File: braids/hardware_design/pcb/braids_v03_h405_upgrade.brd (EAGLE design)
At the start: 78.7 x 106.7 mm, 97 parts, among them IC1 74HC595D, IC2 74HC595D, IC3 LM4040B25, IC4 LM4040B10, IC5 DAC8551, IC6 LM1117-5.0, IC8 MCP6004, IC9 TL072, Q1 MMBT3904, Q2 MMBT3904, Q3 MMBT3904, Q4 MMBT3904, Q6 MMBT3904, SW1 EC12E_SW

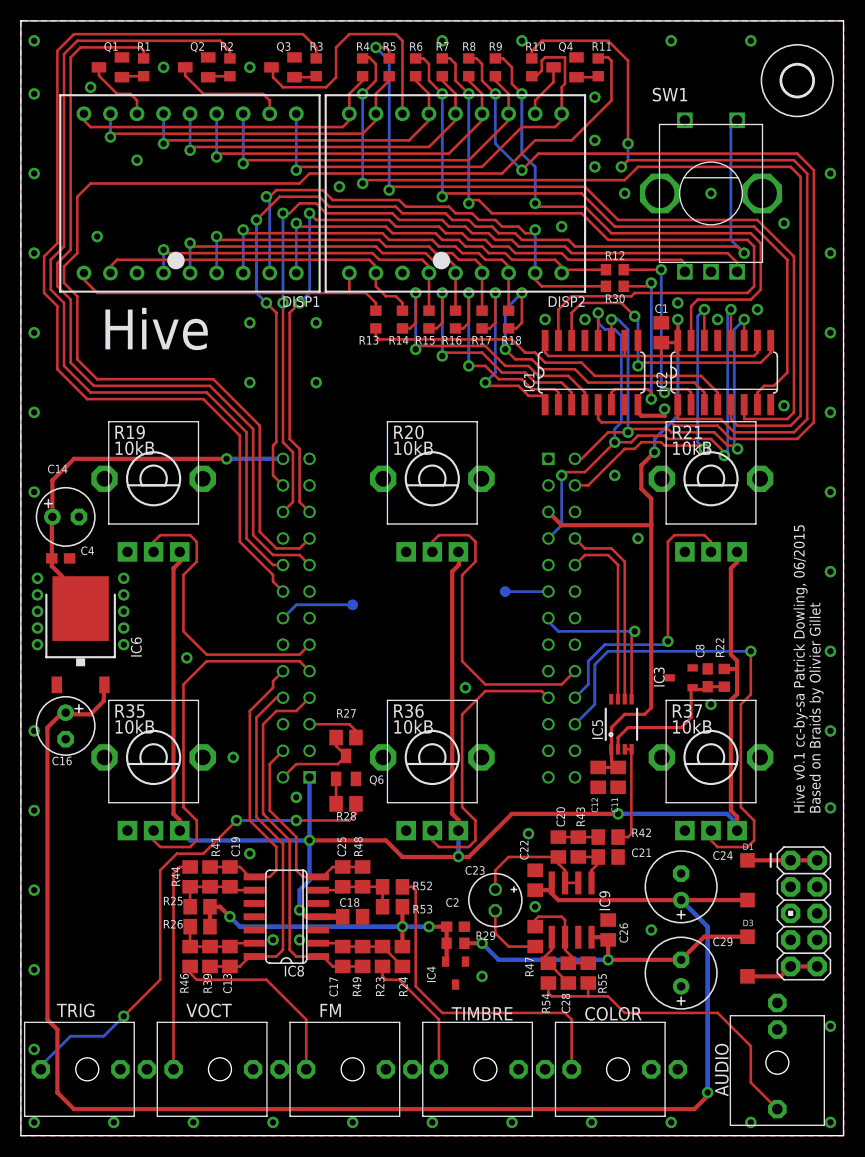
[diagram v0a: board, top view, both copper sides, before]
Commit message: Add switches and LEDs, DAC uses +3V3_A
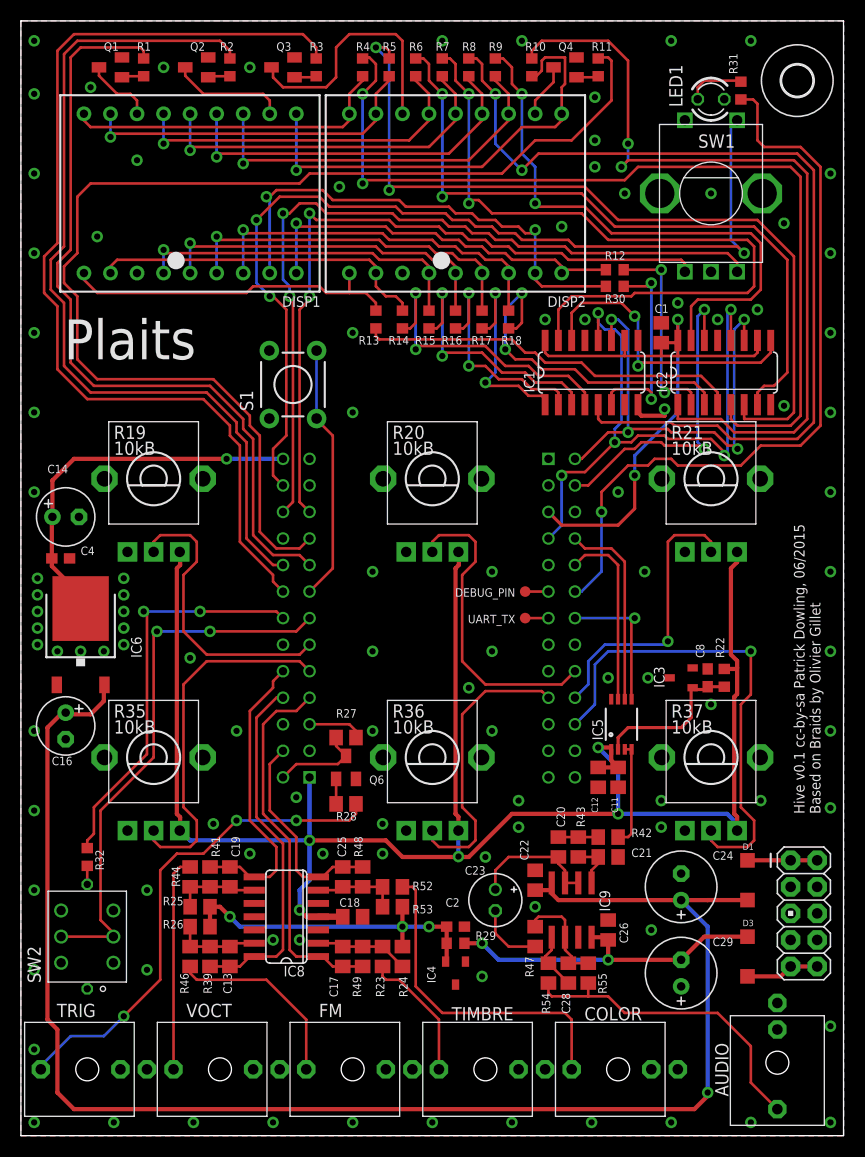
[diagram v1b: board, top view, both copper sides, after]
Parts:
- added LED1: (no value), led:LED3MM
- added R31, R32: 100, rcl:R0603
- added S1: (no value), SparkFun:TACTILE-PTH
- added SW2: LP4OA1PBCT, og-switch:LP4OA1PBCT
- moved TP1 16.6 mm to (48.3, 49.5), flipped to the top
- moved TP2 1.91 mm to (48.3, 52.1), flipped to the top, turned to 270 degrees
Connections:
- removed net 3V3A: C18.1, IC8.4, MCU.EXT2-1, R19.P$1, R20.P$1, R21.P$1, R22.1, R35.P$1, R36.P$1, R37.P$1
- new net +3V3_A: C11.1, C12.1, C18.1, IC5.1, IC8.4, MCU.EXT2-1, R19.P$1, R20.P$1, R21.P$1, R22.1, R35.P$1, R36.P$1, R37.P$1
- new net LED1: MCU.EXT1-12, R31.1
- new net LED2: MCU.EXT2-14, R32.2
- new net N$47: LED1.A, R31.2
- new net N$48: R32.1, SW2.L1
- new net SWITCH1: MCU.EXT2-15, S1.3, S1.4
- new net SWITCH2: MCU.EXT2-13, SW2.P2, SW2.P5
- net +3V3: no longer C11.1, C12.1, IC5.1
- net DAC_SS: now also MCU.EXT1-14; no longer MCU.EXT1-13
- net GND: now also LED1.K, S1.1, S1.2, SW2.L2, SW2.P3, SW2.P6
- net UART_LOGGER: now also MCU.EXT1-13; no longer MCU.EXT2-14
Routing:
- net +3V3_A: track 0.00 -> 174.5 mm, vias 0 -> 5
- net 3V3A: track 162.9 -> 0.00 mm, vias 4 -> 0
- net LED1: track 0.00 -> 72.2 mm, vias 0 -> 1
- net SWITCH2: track 0.00 -> 52.1 mm, vias 0 -> 2
- net LED2: track 0.00 -> 38.7 mm, vias 0 -> 2
- net +3V3: track 91.1 -> 60.1 mm
- net SWITCH1: track 0.00 -> 24.6 mm
- net N$47: track 0.00 -> 5.58 mm
- net UART_LOGGER: track 7.19 -> 2.22 mm
- net DAC_SS: track 15.6 -> 13.6 mm
- net DEBUG_PIN: track 4.13 -> 2.22 mm
- net N$48: track 0.00 -> 1.77 mm
- net ENC_CLICK: track 90.0 -> 91.0 mm
- net ENC_B: track 68.9 -> 68.1 mm
- net N$19: track 32.1 -> 32.7 mm
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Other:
- board text added: "Plaits"
- board text removed: "Hive"

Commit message: Re-assign some GPIOs due to conflicts on Olimex boards, some tweaks
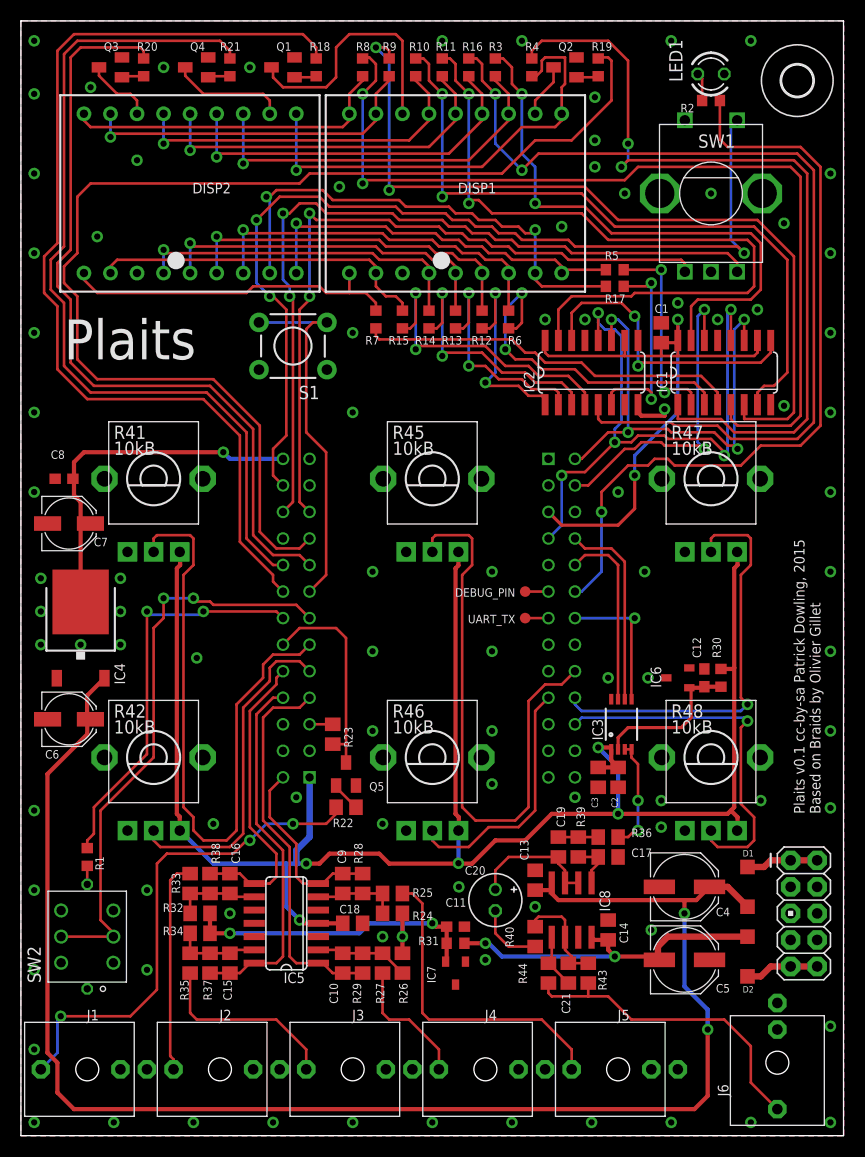
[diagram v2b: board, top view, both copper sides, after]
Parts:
- removed C22, C26: 100n, rcl:C0805
- removed C23: 10u, rcl:E2-5
- removed C24, C29: 47u, rcl:E2,5-7
- removed C25: 1n, rcl:C0805
- removed C28: 47p, rcl:C0805
- removed IC9: TL072, linear:SO08
- removed Q6: MMBT3904, transistor:SOT23-BEC
- removed R49: 66.5k, rcl:R0805
- removed R52, R55: 100k, rcl:R0805
- removed R53: 200k, rcl:R0805
- removed R54: 1k, rcl:R0805
- added C10, C15, C9: 1n, rcl:C0805
- added C3: 1u, rcl:C0805
- added C5: 47u, rcl:PANASONIC_D
- added C6, C7: 22u, rcl:PANASONIC_C
- added IC7: LM4040B10, texas:DBZ_R-PDSO-G3
- added Q5: MMBT3904, transistor:SOT23-BEC
- added R33: 100k, rcl:R0805
- added R34: 200k, rcl:R0805
- added R38: 33k, rcl:R0805
- added R40: 24.9k, rcl:R0805
- added R45: 10kB, pot-alps:ALPS_POT_VERTICAL_PS
- C11: device rcl:C0805 -> rcl:C0603
- C12: value 1u -> 470n; device rcl:C0805 -> rcl:C0603
- C13: value 1n -> 100n
- C14: value 22u -> 100n; device rcl:E2,5-6 -> rcl:C0805
- C16: value 22u -> 1n; device rcl:E2,5-6 -> rcl:C0805
- C17, C19: value 1n -> 100p
- C2: device rcl:C0603 -> rcl:C0805
- C20: value 100p -> 10u; device rcl:C0805 -> rcl:E2-5
- C21: value 100p -> 47p
- C4: value 100n -> 47u; device rcl:C0603 -> rcl:PANASONIC_D
- C8: value 470n -> 100n
- IC3: value LM4040B25 -> DAC8551; device texas:DBZ_R-PDSO-G3 -> og-dac:MSOP-8
- IC4: value LM4040B10 -> LM1117-5.0; device texas:DBZ_R-PDSO-G3 -> og-vreg:TO252
- IC5: value DAC8551 -> MCP6004; device og-dac:MSOP-8 -> gm-ics:SO14
- IC6: value LM1117-5.0 -> LM4040B25; device og-vreg:TO252 -> texas:DBZ_R-PDSO-G3
- IC8: value MCP6004 -> TL072; device gm-ics:SO14 -> linear:SO08
- MCU1: value STM32H103 -> STM32H405
- R1, R11, R2, R3: value 1k -> 100
- R18: value 100 -> 1k
- R19, R20, R21: value 10kB -> 1k; device pot-alps:ALPS_POT_VERTICAL_PS -> rcl:R0603
- R22: value 150 -> 100k; device rcl:R0603 -> rcl:R0805
- R23: value 100k -> 10k
- R27: value 10k -> 100k
- R28: value 100k -> 33k
- R29: value 470 -> 33k; device rcl:R0603 -> rcl:R0805
- R30: value 100 -> 150
- R31: value 100 -> 470
- R32: value 100 -> 100k; device rcl:R0603 -> rcl:R0805
- R35: value 10kB -> 100k; device pot-alps:ALPS_POT_VERTICAL_PS -> rcl:R0805
- R36: value 10kB -> 39k; device pot-alps:ALPS_POT_VERTICAL_PS -> rcl:R0805
- R37: value 10kB -> 33k; device pot-alps:ALPS_POT_VERTICAL_PS -> rcl:R0805
- R39: value 33k -> 39k
- R41: value 33k -> 10kB; device rcl:R0805 -> pot-alps:ALPS_POT_VERTICAL_PS
- R42: value 39k -> 10kB; device rcl:R0805 -> pot-alps:ALPS_POT_VERTICAL_PS
- R43: value 39k -> 100k
- R44: value 100k -> 1k
- R46: value 100k -> 10kB; device rcl:R0805 -> pot-alps:ALPS_POT_VERTICAL_PS
- R47: value 24.9k -> 10kB; device rcl:R0805 -> pot-alps:ALPS_POT_VERTICAL_PS
- R48: value 66.5k -> 10kB; device rcl:R0805 -> pot-alps:ALPS_POT_VERTICAL_PS
- moved R31 86.0 mm to (41.6, 18.4), turned to 180 degrees
- moved R1 75.8 mm to (6.35, 26.7), turned to 90 degrees
- moved C4 67.5 mm to (63.5, 23.8)
- moved C14 65.2 mm to (56.2, 19.7), turned to 270 degrees
- moved C8 64.5 mm to (4.13, 62.9), turned to 180 degrees
- moved R21 60.6 mm to (20.0, 102.2), turned to 270 degrees
- moved R19 58.0 mm to (55.2, 102.2), turned to 270 degrees
- moved IC6 57.3 mm to (62.9, 43.8), turned to 90 degrees
- moved R37 51.8 mm to (18.1, 16.5), turned to 270 degrees
- moved IC4 48.8 mm to (5.71, 48.6), turned to 0 degrees
- moved R20 48.1 mm to (11.7, 102.2), turned to 270 degrees
- moved R47 46.9 mm to (66.0, 62.9), turned to 180 degrees
- moved R2 46.1 mm to (66.0, 99.1), turned to 180 degrees
- moved R42 44.2 mm to (12.7, 36.2), turned to 180 degrees
- moved R30 38.8 mm to (67.0, 43.8), turned to 270 degrees
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- renumbered AUDIO to J6, COLOR to J5, D3 to D2, FM to J3, JP2 to JP1, MCU to MCU1, TIMBRE to J4, TRIG to J1, VOCT to J2
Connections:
- removed net AREF: C8.1, IC3.1, IC5.2, R22.2
- removed net FINE_POT: MCU1.EXT2-11, R19.P$2
- removed net FM_ATT: MCU1.EXT1-20, R21.P$2
- removed net N$11: J2.P3, R44.1
- removed net N$12: J3.P3, R46.1
- removed net N$37 (its old number): IC2.5, R4.1
- removed net N$7: J5.P3, R52.1
- removed net N$8: J4.P3, R23.1
- removed net PARAM1_ATT: MCU1.EXT1-19, R36.P$2
- removed net PARAM1_POT: MCU1.EXT2-9, R35.P$2
- removed net PARAM2_POT: MCU1.EXT1-22, R37.P$2
- removed net PITCH_POT: MCU1.EXT1-18, R20.P$2
- new net ADC_POT1: MCU1.EXT2-11, R41.P$2
- new net ADC_POT2: MCU1.EXT1-18, R45.P$2
- new net ADC_POT3: MCU1.EXT1-20, R47.P$2
- new net ADC_POT4: MCU1.EXT2-9, R42.P$2
- new net ADC_POT5: MCU1.EXT1-19, R46.P$2
- new net ADC_POT6: MCU1.EXT1-22, R48.P$2
- new net AREF_2.5: C12.1, IC3.2, IC6.1, R30.2
- new net COLOR: J5.P3, R25.1
- new net FM: J3.P3, R35.1
- new net N$44: IC2.5, R16.1
- new net TIMBRE: J4.P3, R27.1
- new net VOCT: J2.P3, R33.1
- net +3V3_2: now also R23.2; no longer R27.2
- net +3V3_A: now also C2.1, C3.1, IC3.1, IC5.4, R30.1, R41.P$1, R42.P$1, R45.P$1, R46.P$1, R47.P$1, R48.P$1; no longer C11.1, C12.1, IC5.1, IC8.4, R19.P$1, R20.P$1, R21.P$1, R22.1, R35.P$1, R36.P$1, R37.P$1
- net +5V: now also C7.+, C8.1, IC4.3; no longer C14.+, C4.1, IC6.3
- net AREF_-10: now also C11.1, IC7.2, R31.2, R32.1, R34.1; no longer C2.1, IC4.2, R25.1, R29.2, R53.1
- net AUDIO_OUT: now also IC3.3, IC3.4, R36.2; no longer IC5.3, IC5.4, R42.2
- net DAC_MOSI: now also IC3.7; no longer IC5.7
- net DAC_SCK: now also IC3.6; no longer IC5.6
- net DAC_SS: now also IC3.5; no longer IC5.5
- net DISP_CHAR0: now also R18.1; no longer R3.1
- net DISP_CHAR1: now also R19.1; no longer R11.1
- net DISP_CHAR2: now also R20.1; no longer R1.1
- net DISP_CHAR3: now also R21.1; no longer R2.1
- net DISP_SER: now also IC1.14; no longer IC2.14
- net FM_CV: now also C15.2, IC5.14, R37.2; no longer C13.2, IC8.14, R39.2
- net GATE: now also MCU1.EXT2-12, Q5.C, R23.1; no longer MCU1.EXT2-2, Q6.C, R27.1
- net GATE_IN: now also Q5.B, R22.2; no longer Q6.B, R28.2
- net GND: now also C13.2, C14.1, C17.2, C3.2, C4.-, C5.+, C6.-, C7.-, IC3.8, IC5.10, IC5.11, IC5.12, IC5.3, IC5.5, IC6.2, IC7.1, Q5.E, R41.P$3, R42.P$3, R45.P$3, R46.P$3, R47.P$3, R48.P$3; no longer C14.-, C16.-, C21.2, C22.2, C24.-, C26.1, C29.+, C4.2, IC3.2, IC5.8, IC6.1, IC8.10, IC8.11, IC8.12, IC8.5, IC9.3, Q6.E, R19.P$3, R20.P$3, R21.P$3, R35.P$3, R36.P$3, R37.P$3
- net LED1: now also R2.1; no longer R31.1
- net LED2: now also R1.2; no longer R32.2
- net N$10: now also Q4.B, R21.2; no longer Q2.B, R2.2
- net N$15: now also R3.2; no longer R9.2
- net N$16: now also R4.2; no longer R10.2
- net N$17: now also R5.2; no longer R12.2
- net N$18: now also R6.2; no longer R18.2
- net N$19: now also R7.2; no longer R13.2
- net N$20: now also R8.2; no longer R4.2
- net N$21: now also R9.2; no longer R5.2
- net N$22: now also R10.2; no longer R6.2
- net N$23: now also R11.2; no longer R7.2
- net N$24: now also R12.2; no longer R17.2
- net N$25: now also R13.2; no longer R16.2
- net N$26: now also R14.2; no longer R15.2
- net N$27: now also R15.2; no longer R14.2
- net N$28: now also R16.2; no longer R8.2
- net N$29: now also R17.2; no longer R30.2
- net N$30: now also IC1.7, R10.1; no longer IC2.7, R6.1
- net N$31: now also IC1.9, IC2.14; no longer IC1.14, IC2.9
- net N$32: now also IC1.15, R3.1; no longer IC2.15, R9.1
- net N$33: now also IC1.1, R4.1; no longer IC2.1, R10.1
- net N$34: now also IC1.2, R5.1; no longer IC2.2, R12.1
- net N$35: now also IC1.3, R6.1; no longer IC2.3, R18.1
- net N$36: now also IC1.4, R7.1; no longer IC2.4, R13.1
- net N$38: now also IC1.6, R9.1; no longer IC2.6, R5.1
- net N$39: now also IC2.15, R11.1; no longer IC1.15, R7.1
- net N$40: now also IC2.1, R12.1; no longer IC1.1, R17.1
- net N$41: now also IC2.2, R13.1; no longer IC1.2, R16.1
- net N$42: now also IC2.3, R14.1; no longer IC1.3, R15.1
- net N$43: now also IC2.4, R15.1; no longer IC1.4, R14.1
- net N$45: now also C9.1, IC5.6, R24.2, R25.2, R28.1; no longer C25.1, IC8.6, R48.1, R52.2, R53.2
- net N$46: now also IC2.6, R17.1; no longer IC1.6, R30.1
- net N$47: now also R2.2; no longer R31.2
- net N$48: now also R1.1; no longer R32.1
- net N$5: now also Q1.B, R18.2; no longer Q3.B, R3.2
- net N$50: now also C15.1, IC5.13, R34.2, R35.2, R37.1; no longer C13.1, IC8.13, R26.2, R39.1, R46.2
- net N$52: now also C10.1, IC5.2, R26.2, R27.2, R29.1; no longer C17.1, IC8.2, R23.2, R24.2, R49.1
- net N$57: now also R22.1; no longer R28.1
- net N$6: now also Q2.B, R19.2; no longer Q4.B, R11.2
- net N$63: now also C16.1, IC5.9, R32.2, R33.2, R38.1; no longer C19.1, IC8.9, R25.2, R41.1, R44.2
- net N$67: now also C19.2, C20.+, IC8.6, IC8.7; no longer C20.2, C23.+, IC9.6, IC9.7
- net N$68: now also C20.-, R40.2; no longer C23.-, R47.2
- net N$69: now also C17.1, IC8.5, R39.1; no longer C21.1, IC9.5, R43.1
- net N$71: now also C19.1, R36.1, R39.2; no longer C20.1, R42.1, R43.2
- net N$72: now also R43.1, R44.1; no longer R54.1, R55.1
- net N$73: now also C21.2, IC8.1, R44.2; no longer C28.2, IC9.1, R54.2
- net N$75: now also C21.1, IC8.2, R40.1, R43.2; no longer C28.1, IC9.2, R47.1, R55.2
- net N$9: now also Q3.B, R20.2; no longer Q1.B, R1.2
- net PARAM1_CV: now also C10.2, IC5.1, R29.2; no longer C17.2, IC8.1, R49.2
- net PARAM2_CV: now also C9.2, IC5.7, MCU1.EXT2-2, R28.2; no longer C25.2, IC8.7, MCU1.EXT2-4, R48.2
- net PITCH_CV: now also C16.2, IC5.8, R38.2; no longer C19.2, IC8.8, R41.2
- net VCC: now also C13.1, C4.+, C6.+, IC4.2, IC8.8; no longer C16.+, C22.1, C24.+, IC6.2, IC9.8
- net VEE: now also C14.2, C5.-, IC8.4, R31.1; no longer C26.2, C29.-, IC9.4, R29.1
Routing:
- net N$44: track 0.00 -> 90.1 mm, vias 0 -> 2
- net N$37 (its old number): track 88.1 -> 0.00 mm, vias 2 -> 0
- net ADC_POT1: track 0.00 -> 61.2 mm
- net ADC_POT2: track 0.00 -> 54.7 mm
- net PARAM2_POT: track 46.6 -> 0.00 mm, vias 1 -> 0
- net ADC_POT3: track 0.00 -> 39.6 mm, vias 0 -> 1
- net ADC_POT6: track 0.00 -> 34.7 mm, vias 0 -> 1
- net PARAM1_POT: track 34.4 -> 0.00 mm
- net ADC_POT4: track 0.00 -> 31.7 mm
- net N$7: track 31.6 -> 0.00 mm
- net COLOR: track 0.00 -> 30.4 mm
- net PITCH_POT: track 29.8 -> 0.00 mm
- net FINE_POT: track 28.1 -> 0.00 mm
- net PARAM1_ATT: track 27.6 -> 0.00 mm
- net FM_ATT: track 27.6 -> 0.00 mm, vias 1 -> 0
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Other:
- board text added: "Plaits v0.1 cc-by-sa Patrick Dowling, 2015 Based on Braids by Olivier Gillet"
- board text removed: "Hive v0.1 cc-by-sa Patrick Dowling, 06/2015 Based on Braids by Olivier Gillet"

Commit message: Tweaks
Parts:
- moved C3 2.22 mm to (57.5, 34.3)
- moved C2 1.59 mm to (55.6, 34.3)
- moved R23 0.32 mm to (30.2, 38.4)
- moved TP1 0.32 mm to (48.6, 49.5)
- moved TP2 0.32 mm to (48.6, 52.1)
- moved MCU1 0.32 mm to (39.4, 49.5)
- turned S1 to 0 degrees
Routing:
- net ENC_CLICK: track 91.0 -> 97.0 mm
- net SWITCH2: track 55.2 -> 52.9 mm
- net DISP_CHAR1: track 112.9 -> 113.9 mm
- net DISP_CHAR2: track 75.3 -> 76.4 mm
- net DISP_CHAR3: track 83.2 -> 84.3 mm
- net DISP_CHAR0: track 95.3 -> 96.1 mm
- net ADC_POT5: track 23.8 -> 24.5 mm
- net GATE: track 20.3 -> 19.7 mm
- net N$19: track 32.7 -> 32.1 mm
- net +3V3_A: track 173.9 -> 174.4 mm
- net SWITCH1: track 35.3 -> 35.6 mm, vias 0 -> 1
- net GND: vias 92 -> 93

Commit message: Yet another GPIO re-assign...
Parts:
- moved R23 3.62 mm to (31.1, 34.9), turned to 180 degrees
- moved R22 2.54 mm to (31.1, 28.9)
- moved Q5 2.54 mm to (31.1, 32.1)
- moved C13 0.71 mm to (49.5, 23.8)
- moved C17 0.71 mm to (56.5, 26.0)
- moved IC8 0.71 mm to (53.0, 21.0)
- moved R40 0.71 mm to (49.5, 18.4)
- moved R43 0.71 mm to (54.6, 14.9)
- moved C20 0.71 mm to (45.7, 21.9)
- moved C14 0.71 mm to (56.5, 19.1)
- moved R36 0.71 mm to (56.5, 27.9)
- moved C21 0.71 mm to (52.7, 14.9)
- moved R44 0.71 mm to (50.8, 14.9)
- moved C19 0.71 mm to (51.8, 27.0)
- moved R39 0.71 mm to (53.7, 27.0)
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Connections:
- net GATE: now also MCU1.EXT2-2; no longer MCU1.EXT2-12
- net PARAM2_CV: now also MCU1.EXT1-26; no longer MCU1.EXT2-2
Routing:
- net PARAM2_CV: track 18.0 -> 31.0 mm, vias 0 -> 2
- net GATE: track 19.7 -> 9.01 mm
- net +3V3_2: track 2.22 -> 6.11 mm
- net ADC_POT2: track 55.0 -> 53.4 mm
- net VCC: track 148.5 -> 147.8 mm
- net AUDIO_OUT: track 11.1 -> 11.8 mm
- net N$72: track 30.8 -> 30.2 mm
- net +3V3_A: track 174.4 -> 173.8 mm
- net ADC_POT5: track 24.5 -> 25.1 mm
- net GND: vias 93 -> 92
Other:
- board text added: "Buckle up..."
